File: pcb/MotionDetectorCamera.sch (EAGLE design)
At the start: 138 parts, among them J2 S-MOUNT-LENS-HOLDER, J3 MINI-USB-JACK, U1 LATTICE-ICE40HX4K-BG121, U10 NXP-NTB0102, U11 ON-NLAS3157, U12 ON-NLAS3157, U13 STM-STM32F730, U2 TI-TPS6280XYKAR, U22 TI-TPD4S012DRYR, U3 MICROSD-SOCKET, U4 TI-TPS6280XYKAR, U5 W989D6DBGX6I, U6 TI-TPS63805YFFR, U8 ON-AR0330CS1C12SPKA0, U9 TI-TMUX1574, X1 SITIME-SIT8021, X2 SITIME-SIT8021

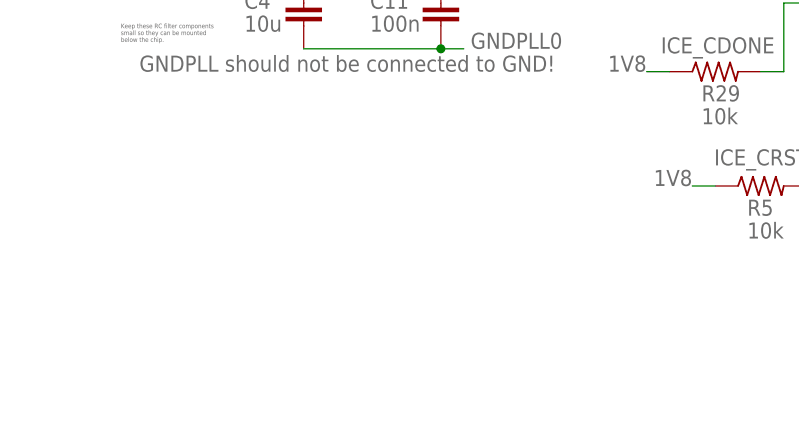
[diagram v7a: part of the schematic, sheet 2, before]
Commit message: Adjust vias
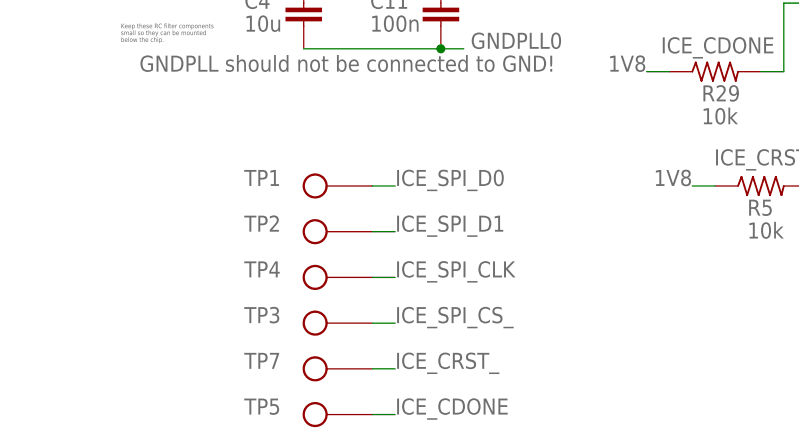
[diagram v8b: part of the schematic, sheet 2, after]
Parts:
- added TP1, TP2, TP3, TP4, TP5, TP7: TEST-POINT, EagleLibrary:TEST-POINT
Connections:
- net ICE_CDONE: now also TP5.X
- net ICE_CRST_: now also TP7.X
- net ICE_SPI_CLK: now also TP4.X
- net ICE_SPI_CS_: now also TP3.X
- net ICE_SPI_D0: now also TP1.X
- net ICE_SPI_D1: now also TP2.X
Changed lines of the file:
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@@
 <attribute name="PN" value="C0805C106K8PACTU"/>
 </part>
+<part name="TP1" library="EagleLibrary" deviceset="TEST-POINT" device=""/>
+<part name="TP2" library="EagleLibrary" deviceset="TEST-POINT" device=""/>
+<part name="TP3" library="EagleLibrary" deviceset="TEST-POINT" device=""/>
+<part name="TP4" library="EagleLibrary" deviceset="TEST-POINT" device=""/>
+<part name="TP5" library="EagleLibrary" deviceset="TEST-POINT" device=""/>
+<part name="TP7" library="EagleLibrary" deviceset="TEST-POINT" device=""/>
 </parts>
 <sheets>
@@
 <attribute name="MFG" x="68.58" y="-101.6" size="1.778" layer="96" display="off"/>
 <attribute name="PN" x="68.58" y="-101.6" size="1.778" layer="96" display="off"/>
+</instance>
+<instance part="TP1" gate="G$1" x="30.48" y="-114.3" smashed="yes" rot="R180">
+<attribute name="NAME" x="20.32" y="-114.3" size="1.778" layer="95" align="bottom-right"/>
+</instance>
+<instance part="TP2" gate="G$1" x="30.48" y="-119.38" smashed="yes" rot="R180">
+<attribute name="NAME" x="20.32" y="-119.38" size="1.778" layer="95" align="bottom-right"/>
+</instance>
+<instance part="TP3" gate="G$1" x="30.48" y="-129.54" smashed="yes" rot="R180">
+<attribute name="NAME" x="20.32" y="-129.54" size="1.778" layer="95" align="bottom-right"/>
+</instance>
+<instance part="TP4" gate="G$1" x="30.48" y="-124.46" smashed="yes" rot="R180">
+<attribute name="NAME" x="20.32" y="-124.46" size="1.778" layer="95" align="bottom-right"/>
+</instance>
+<instance part="TP5" gate="G$1" x="30.48" y="-139.7" smashed="yes" rot="R180">
+<attribute name="NAME" x="20.32" y="-139.7" size="1.778" layer="95" align="bottom-right"/>
+</instance>
+<instance part="TP7" gate="G$1" x="30.48" y="-134.62" smashed="yes" rot="R180">
+<attribute name="NAME" x="20.32" y="-134.62" size="1.778" layer="95" align="bottom-right"/>
 </instance>
 </instances>
@@
 <pinref part="R29" gate="G$1" pin="2"/>
 </segment>
+<segment>
+<pinref part="TP5" gate="G$1" pin="X"/>
+<wire x1="30.48" y1="-139.7" x2="33.02" y2="-139.7" width="0.1524" layer="91"/>
+<label x="33.02" y="-139.7" size="1.778" layer="95"/>
+</segment>
 </net>
 <net name="ICE_CRST_" class="0">
@@
 <wire x1="81.28" y1="-114.3" x2="81.28" y2="-96.52" width="0.1524" layer="91"/>
 </segment>
+<segment>
+<pinref part="TP7" gate="G$1" pin="X"/>
+<wire x1="30.48" y1="-134.62" x2="33.02" y2="-134.62" width="0.1524" layer="91"/>
+<label x="33.02" y="-134.62" size="1.778" layer="95"/>
+</segment>
 </net>
 <net name="ICE_SPI_D1" class="0">
@@
 <label x="80.772" y="-83.82" size="1.778" layer="95" rot="MR0"/>
 </segment>
+<segment>
+<pinref part="TP2" gate="G$1" pin="X"/>
+<wire x1="30.48" y1="-119.38" x2="33.02" y2="-119.38" width="0.1524" layer="91"/>
+<label x="33.02" y="-119.38" size="1.778" layer="95"/>
+</segment>
 </net>
 <net name="ICE_SPI_D0" class="0">
@@
 <label x="80.772" y="-81.28" size="1.778" layer="95" rot="MR0"/>
 </segment>
+<segment>
+<pinref part="TP1" gate="G$1" pin="X"/>
+<wire x1="30.48" y1="-114.3" x2="33.02" y2="-114.3" width="0.1524" layer="91"/>
+<label x="33.02" y="-114.3" size="1.778" layer="95"/>
+</segment>
 </net>
 <net name="ICE_SPI_CLK" class="0">
@@
 <label x="80.772" y="-88.9" size="1.778" layer="95" rot="MR0"/>
 </segment>
+<segment>
+<pinref part="TP4" gate="G$1" pin="X"/>
+<wire x1="30.48" y1="-124.46" x2="33.02" y2="-124.46" width="0.1524" layer="91"/>
+<label x="33.02" y="-124.46" size="1.778" layer="95"/>
+</segment>
 </net>
 <net name="ICE_SPI_CS_" class="0">
@@
 <label x="80.772" y="-86.36" size="1.778" layer="95" rot="MR0"/>
 </segment>
-</net>
+<segment>
+<pinref part="TP3" gate="G$1" pin="X"/>
+<wire x1="30.48" y1="-129.54" x2="33.02" y2="-129.54" width="0.1524" layer="91"/>
+<label x="33.02" y="-129.54" size="1.778" layer="95"/>
+</segment>
+</net>
